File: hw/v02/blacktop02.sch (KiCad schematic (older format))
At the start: 12 parts, among them J1 Conn_01x10_Female_Left, J2 Conn_01x10_Female_Right, SW1 EVQ-Q2Y03W, U1 MSP430G2553IPW28, U2 AT25640B-SSHL-T, U3 HDSM-283L, U4 HDSM-283L, U5 HDSM-283L, U6 HDSM-283L

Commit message: v03 RC1 (rename is nontrivial so use v02 dir)
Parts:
- added FID1, FID2, FID3: Fiducial, Fiducial:Fiducial_0.75mm_Mask1.5mm, symbol blacktop01:Fiducial
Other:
- moved on the sheet: RV1
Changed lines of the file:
@@
 L Device:R_POT_US RV1
 U 1 1 5E325DF6
-P 10500 1700
-F 0 "RV1" V 10295 1700 50  0000 C CNN
-F 1 "10k" V 10400 1700 50  0000 C CNN
-F 2 "blacktop01:PTV09A-4020U-B103" H 10500 1700 50  0001 C CNN
-F 3 "https://www.bourns.com/docs/product-datasheets/PTV09.pdf" H 10500 1700 50  0001 C CNN
-	1    10500 1700
+P 10500 2250
+F 0 "RV1" V 10295 2250 50  0000 C CNN
+F 1 "10k" V 10400 2250 50  0000 C CNN
+F 2 "blacktop01:PTV09A-4020U-B103" H 10500 2250 50  0001 C CNN
+F 3 "https://www.bourns.com/docs/product-datasheets/PTV09.pdf" H 10500 2250 50  0001 C CNN
+	1    10500 2250
 	0    1    1    0
 $EndComp
@@
 	2500 3300 1400 3300
 Wire Wire Line
-	10500 1850 10500 1900
-Wire Wire Line
-	10650 1700 10750 1700
-Wire Wire Line
-	10750 1900 10500 1900
-Connection ~ 10500 1900
-Wire Wire Line
-	10500 1900 10500 2700
+	10500 2400 10500 2450
+Wire Wire Line
+	10650 2250 10750 2250
+Wire Wire Line
+	10750 2450 10500 2450
+Connection ~ 10500 2450
+Wire Wire Line
+	10500 2450 10500 2700
 $Comp
 L power:VCC #PWR0108
 U 1 1 5E3334B9
-P 10150 1600
-F 0 "#PWR0108" H 10150 1450 50  0001 C CNN
-F 1 "VCC" H 10167 1773 50  0000 C CNN
-F 2 "" H 10150 1600 50  0001 C CNN
-F 3 "" H 10150 1600 50  0001 C CNN
-	1    10150 1600
+P 10150 2150
+F 0 "#PWR0108" H 10150 2000 50  0001 C CNN
+F 1 "VCC" H 10167 2323 50  0000 C CNN
+F 2 "" H 10150 2150 50  0001 C CNN
+F 3 "" H 10150 2150 50  0001 C CNN
+	1    10150 2150
 	1    0    0    -1
 $EndComp
 Wire Wire Line
-	10150 1600 10150 1700
-Wire Wire Line
-	10150 1700 10350 1700
+	10150 2150 10150 2250
+Wire Wire Line
+	10150 2250 10350 2250
 Wire Wire Line
 	9300 3700 10200 3700
@@
 	8000 1300 2600 1300
 Wire Wire Line
-	10750 1700 10750 1900
+	10750 2250 10750 2450
 Wire Wire Line
 	2500 1000 2500 3300
@@
 NoConn ~ 3000 7000
 NoConn ~ 1700 7000
+Text Label 10700 7650 2    50   ~ 0
+03
+$Comp
+L blacktop01:Fiducial FID1
+U 1 1 5E5190CE
+P 10150 850
+F 0 "FID1" H 10235 896 50  0000 L CNN
+F 1 "Fiducial" H 10235 805 50  0000 L CNN
+F 2 "Fiducial:Fiducial_0.75mm_Mask1.5mm" H 10150 850 50  0001 C CNN
+F 3 "~" H 10150 850 50  0001 C CNN
+	1    10150 850
+	1    0    0    -1
+$EndComp
+$Comp
+L blacktop01:Fiducial FID2
+U 1 1 5E5198D0
+P 10150 1100
+F 0 "FID2" H 10235 1146 50  0000 L CNN
+F 1 "Fiducial" H 10235 1055 50  0000 L CNN
+F 2 "Fiducial:Fiducial_0.75mm_Mask1.5mm" H 10150 1100 50  0001 C CNN
+F 3 "~" H 10150 1100 50  0001 C CNN
+	1    10150 1100
+	1    0    0    -1
+$EndComp
+$Comp
+L blacktop01:Fiducial FID3
+U 1 1 5E519B76
+P 10150 1350
+F 0 "FID3" H 10235 1396 50  0000 L CNN
+F 1 "Fiducial" H 10235 1305 50  0000 L CNN
+F 2 "Fiducial:Fiducial_0.75mm_Mask1.5mm" H 10150 1350 50  0001 C CNN
+F 3 "~" H 10150 1350 50  0001 C CNN
+	1    10150 1350
+	1    0    0    -1
+$EndComp
 $EndSCHEMATC

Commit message: moved RV1 pin3 from pin2 to GND
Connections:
- net GND: now also RV1.1
- net POT: no longer RV1.1
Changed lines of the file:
@@
 	2500 3300 1400 3300
 Wire Wire Line
-	10500 2400 10500 2450
-Wire Wire Line
 	10650 2250 10750 2250
-Wire Wire Line
-	10750 2450 10500 2450
-Connection ~ 10500 2450
-Wire Wire Line
-	10500 2450 10500 2700
 $Comp
 L power:VCC #PWR0108
@@
 	1    0    0    -1
 $EndComp
+Wire Wire Line
+	10500 2400 10500 2700
+$Comp
+L power:GND #PWR?
+U 1 1 5E4C0CB2
+P 10750 2450
+F 0 "#PWR?" H 10750 2200 50  0001 C CNN
+F 1 "GND" H 10755 2277 50  0000 C CNN
+F 2 "" H 10750 2450 50  0001 C CNN
+F 3 "" H 10750 2450 50  0001 C CNN
+	1    10750 2450
+	1    0    0    -1
+$EndComp

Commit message: Tied eeprom 3 and 7 to VCC, board v04 RC
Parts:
- FID1, FID2, FID3: symbol blacktop01:Fiducial -> blacktop02-rescue:Fiducial-blacktop01
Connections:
- net VCC: now also U2.3 (~WP), U2.7 (~HOLD)
- no-connect marks 22 -> 20
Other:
- moved on the sheet: C2
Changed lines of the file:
@@
 Text Label 5350 4600 0    50   ~ 0
 P1.6
-NoConn ~ 9600 5600
-NoConn ~ 9600 5500
 NoConn ~ 6500 7000
 NoConn ~ 6350 7000
@@
 L Device:C C2
 U 1 1 5E76B875
-P 9500 5250
-F 0 "C2" V 9248 5250 50  0000 C CNN
-F 1 "0.1UF" V 9339 5250 50  0000 C CNN
-F 2 "Capacitor_SMD:C_0603_1608Metric_Pad1.05x0.95mm_HandSolder" H 9538 5100 50  0001 C CNN
-F 3 "~" H 9500 5250 50  0001 C CNN
-	1    9500 5250
+P 9350 5250
+F 0 "C2" V 9098 5250 50  0000 C CNN
+F 1 "0.1UF" V 9189 5250 50  0000 C CNN
+F 2 "Capacitor_SMD:C_0603_1608Metric_Pad1.05x0.95mm_HandSolder" H 9388 5100 50  0001 C CNN
+F 3 "~" H 9350 5250 50  0001 C CNN
+	1    9350 5250
 	0    1    1    0
 $EndComp
 Wire Wire Line
 	10000 5150 10000 5250
-Wire Wire Line
-	9650 5250 10000 5250
 Connection ~ 10000 5250
 Wire Wire Line
@@
 L power:GND #PWR01
 U 1 1 5E7837AF
-P 9250 5300
-F 0 "#PWR01" H 9250 5050 50  0001 C CNN
-F 1 "GND" H 9255 5127 50  0000 C CNN
-F 2 "" H 9250 5300 50  0001 C CNN
-F 3 "" H 9250 5300 50  0001 C CNN
-	1    9250 5300
+P 9100 5300
+F 0 "#PWR01" H 9100 5050 50  0001 C CNN
+F 1 "GND" H 9105 5127 50  0000 C CNN
+F 2 "" H 9100 5300 50  0001 C CNN
+F 3 "" H 9100 5300 50  0001 C CNN
+	1    9100 5300
 	1    0    0    -1
 $EndComp
 Wire Wire Line
-	9350 5250 9250 5250
-Wire Wire Line
-	9250 5250 9250 5300
+	9200 5250 9100 5250
+Wire Wire Line
+	9100 5250 9100 5300
 $Bitmap
 Pos 9150 6800
@@
 NoConn ~ 1700 7000
 Text Label 10700 7650 2    50   ~ 0
-03
+04
 $Comp
-L blacktop01:Fiducial FID1
+L blacktop02-rescue:Fiducial-blacktop01 FID1
 U 1 1 5E5190CE
 P 10150 850
@@
 $EndComp
 $Comp
-L blacktop01:Fiducial FID2
+L blacktop02-rescue:Fiducial-blacktop01 FID2
 U 1 1 5E5198D0
 P 10150 1100
@@
 $EndComp
 $Comp
-L blacktop01:Fiducial FID3
+L blacktop02-rescue:Fiducial-blacktop01 FID3
 U 1 1 5E519B76
 P 10150 1350
@@
 	1    0    0    -1
 $EndComp
+Wire Wire Line
+	9500 5250 9550 5250
+Wire Wire Line
+	9600 5600 9550 5600
+Wire Wire Line
+	9550 5600 9550 5500
+Connection ~ 9550 5250
+Wire Wire Line
+	9550 5250 10000 5250
+Wire Wire Line
+	9600 5500 9550 5500
+Connection ~ 9550 5500
+Wire Wire Line
+	9550 5500 9550 5250
 $EndSCHEMATC

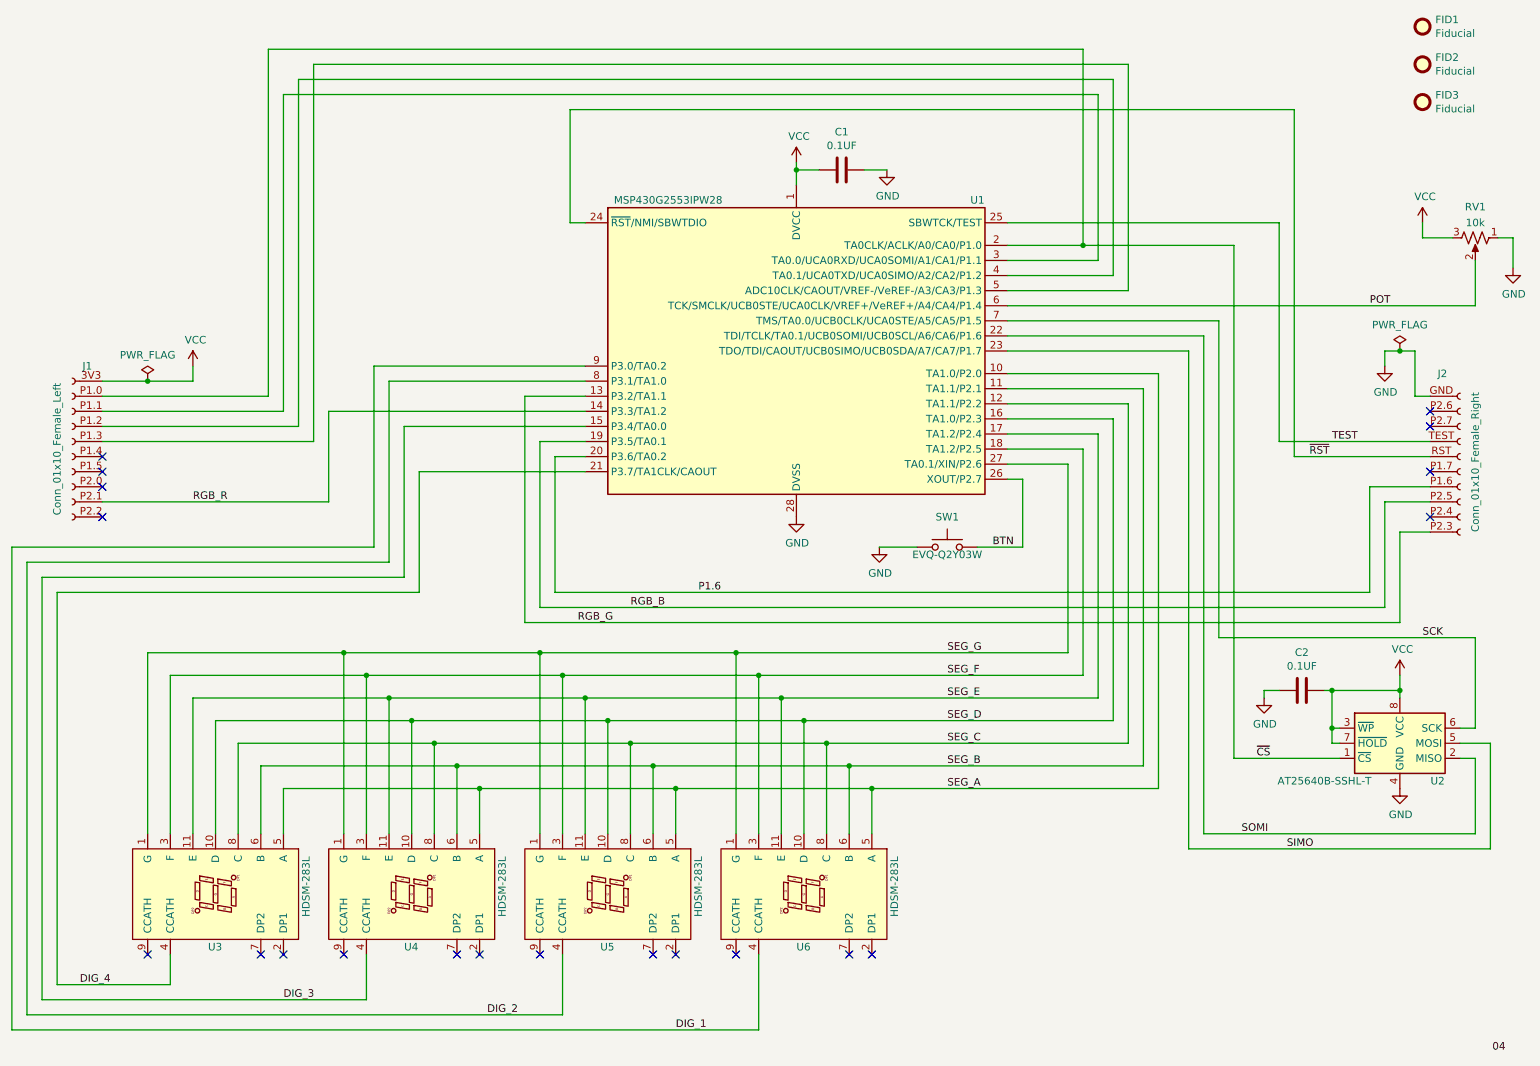
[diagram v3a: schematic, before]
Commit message: added hardware pullup (R1) to BTN
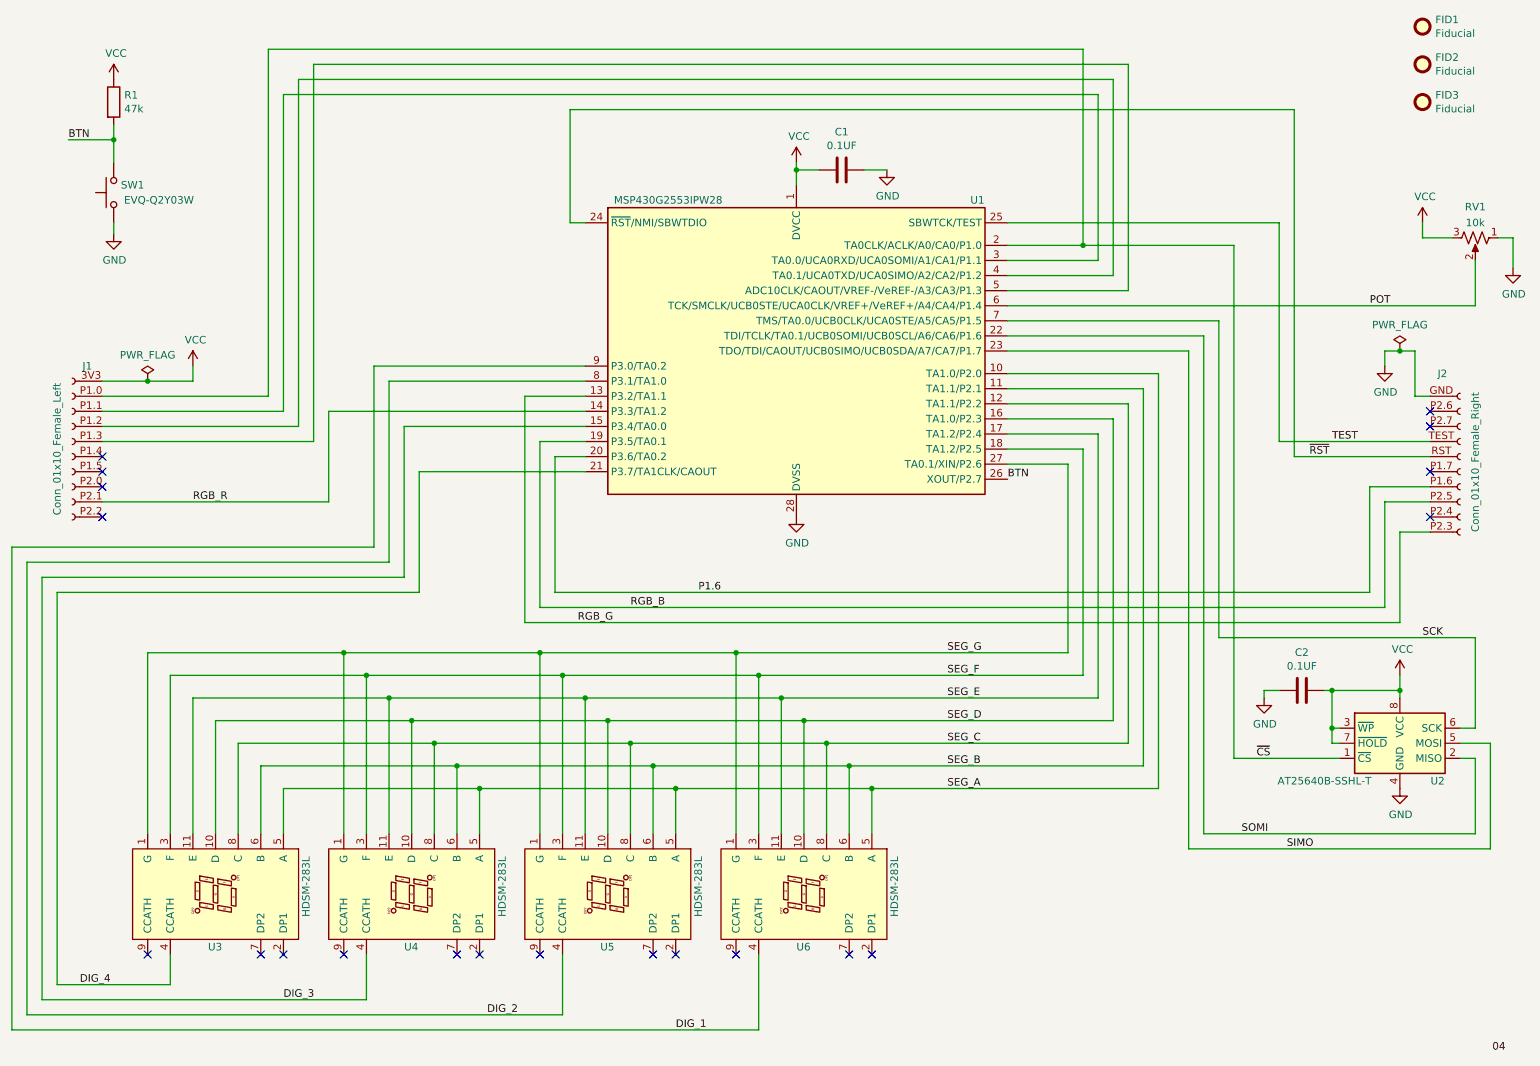
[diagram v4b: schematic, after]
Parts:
- added R1: 47k, Resistor_SMD:R_0603_1608Metric_Pad1.05x0.95mm_HandSolder, symbol Device:R
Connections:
- net BTN: now also R1.2
- net VCC: now also R1.1
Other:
- moved on the sheet: SW1
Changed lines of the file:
@@
 Wire Wire Line
 	10000 4200 10000 4800
-$Comp
-L Switch:SW_Push SW1
-U 1 1 5E68F934
-P 7000 4300
-F 0 "SW1" H 7000 4500 50  0000 C CNN
-F 1 "EVQ-Q2Y03W" H 7000 4250 50  0000 C CNN
-F 2 "Button_Switch_SMD:SW_SPST_EVQQ2" H 7000 4500 50  0001 C CNN
-F 3 "https://industrial.panasonic.com/ac/cdn/e/control/switch/light-touch/catalog/sw_lt_eng_6s_th.pdf" H 7000 4500 50  0001 C CNN
-	1    7000 4300
-	1    0    0    -1
-$EndComp
-Wire Wire Line
-	7200 4300 7500 4300
-Wire Wire Line
-	7500 3850 7400 3850
-Text Label 7300 4300 0    50   ~ 0
+Text Label 7400 3850 0    50   ~ 0
 BTN
 Text Label 2000 4000 0    50   ~ 0
@@
 Wire Wire Line
 	10000 3000 10100 3000
-Wire Wire Line
-	7500 4300 7500 3850
 $Comp
 L power:GND #PWR0109
 U 1 1 5E74421C
-P 6550 4300
-F 0 "#PWR0109" H 6550 4050 50  0001 C CNN
-F 1 "GND" H 6555 4127 50  0000 C CNN
-F 2 "" H 6550 4300 50  0001 C CNN
-F 3 "" H 6550 4300 50  0001 C CNN
-	1    6550 4300
+P 1475 2225
+F 0 "#PWR0109" H 1475 1975 50  0001 C CNN
+F 1 "GND" H 1480 2052 50  0000 C CNN
+F 2 "" H 1475 2225 50  0001 C CNN
+F 3 "" H 1475 2225 50  0001 C CNN
+	1    1475 2225
 	1    0    0    -1
 $EndComp
-Wire Wire Line
-	6550 4300 6800 4300
 Wire Wire Line
 	10500 4900 10500 5500
@@
 	10500 2400 10500 2700
 $Comp
-L power:GND #PWR?
+L power:GND #PWR0110
 U 1 1 5E4C0CB2
 P 10750 2450
-F 0 "#PWR?" H 10750 2200 50  0001 C CNN
+F 0 "#PWR0110" H 10750 2200 50  0001 C CNN
 F 1 "GND" H 10755 2277 50  0000 C CNN
 F 2 "" H 10750 2450 50  0001 C CNN
@@
 Wire Wire Line
 	9550 5500 9550 5250
+Text Label 1175 1600 0    50   ~ 0
+BTN
+$Comp
+L Device:R R1
+U 1 1 5ED2CB50
+P 1475 1350
+F 0 "R1" H 1545 1396 50  0000 L CNN
+F 1 "47k" H 1545 1305 50  0000 L CNN
+F 2 "Resistor_SMD:R_0603_1608Metric_Pad1.05x0.95mm_HandSolder" V 1405 1350 50  0001 C CNN
+F 3 "http://www.vishay.com/docs/28773/crcwce3.pdf" H 1475 1350 50  0001 C CNN
+	1    1475 1350
+	1    0    0    -1
+$EndComp
+$Comp
+L power:VCC #PWR0111
+U 1 1 5ED581EB
+P 1475 1200
+F 0 "#PWR0111" H 1475 1050 50  0001 C CNN
+F 1 "VCC" H 1490 1373 50  0000 C CNN
+F 2 "" H 1475 1200 50  0001 C CNN
+F 3 "" H 1475 1200 50  0001 C CNN
+	1    1475 1200
+	1    0    0    -1
+$EndComp
+$Comp
+L Switch:SW_Push SW1
+U 1 1 5E68F934
+P 1475 1950
+F 0 "SW1" V 1525 1825 50  0000 C CNN
+F 1 "EVQ-Q2Y03W" V 1425 1650 50  0000 C CNN
+F 2 "Button_Switch_SMD:SW_SPST_EVQQ2" H 1475 2150 50  0001 C CNN
+F 3 "https://industrial.panasonic.com/ac/cdn/e/control/switch/light-touch/catalog/sw_lt_eng_6s_th.pdf" H 1475 2150 50  0001 C CNN
+	1    1475 1950
+	0    -1   -1   0
+$EndComp
+Wire Wire Line
+	1475 2150 1475 2225
+Wire Wire Line
+	1175 1600 1475 1600
+Wire Wire Line
+	1475 1500 1475 1600
+Connection ~ 1475 1600
+Wire Wire Line
+	1475 1600 1475 1750
 $EndSCHEMATC
